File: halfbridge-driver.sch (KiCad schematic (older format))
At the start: 33 parts, among them U12 MGJ1, U13 MGJ1, U14 2ED020I12-F2

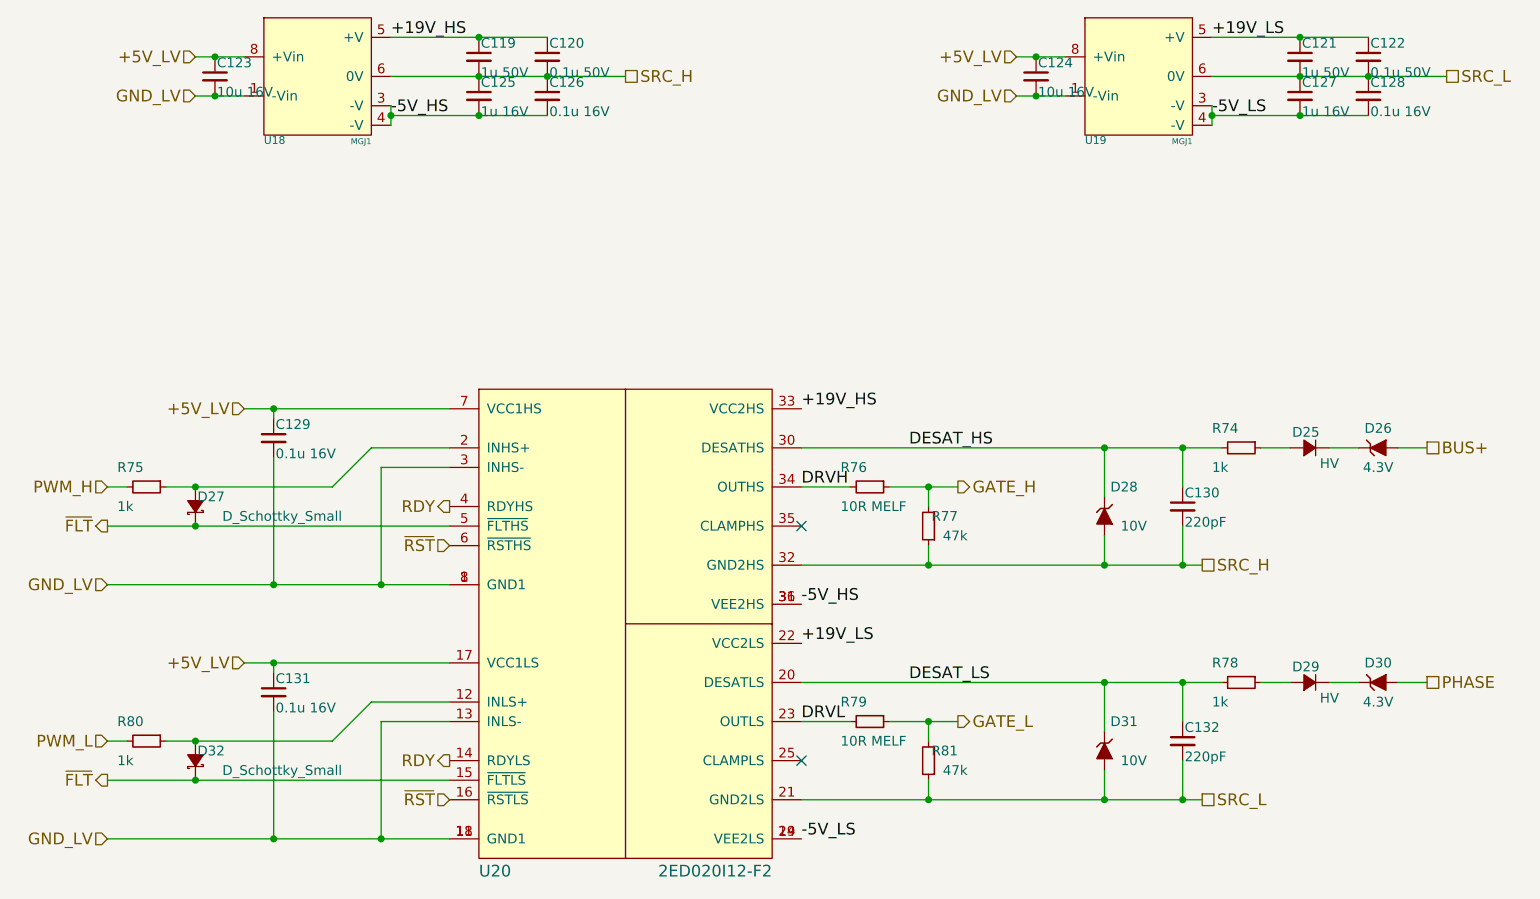
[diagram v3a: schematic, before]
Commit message: Add 1568 vias in DC link cap pads
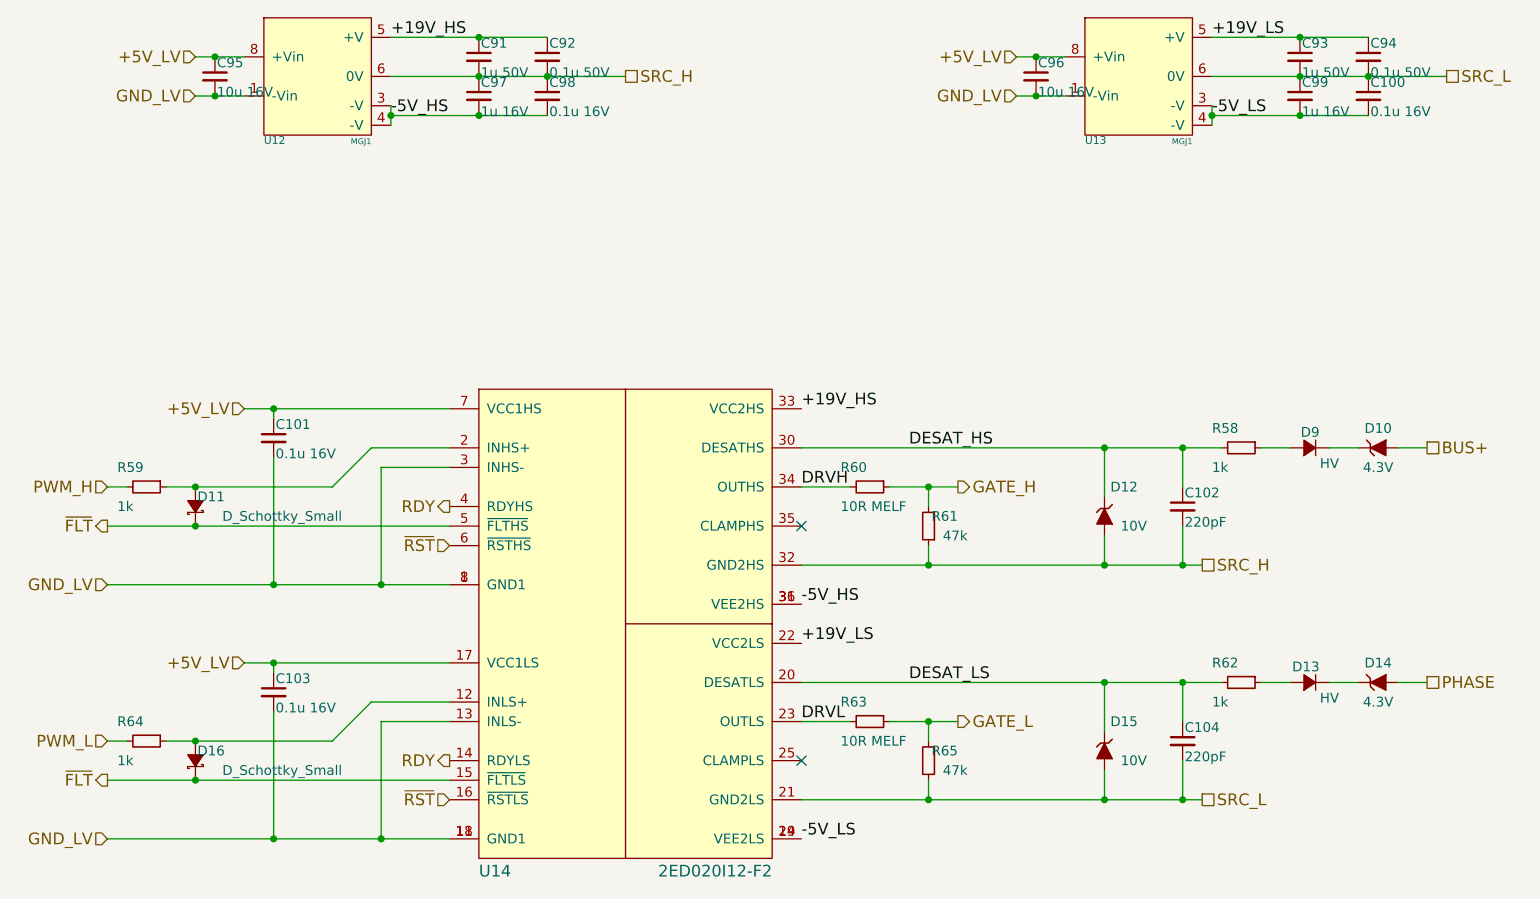
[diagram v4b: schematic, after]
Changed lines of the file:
@@
 AR Path="/57A1662D/57F260F4/57F02200" Ref="U17"  Part="1"
 AR Path="/57A1662D/57F2705F/57F02200" Ref="U20"  Part="1"
-F 0 "U20" H 4450 2750 60  0000 L BNN
+F 0 "U14" H 4450 2750 60  0000 L BNN
 F 1 "2ED020I12-F2" H 5950 2750 60  0000 R BNN
 F 2 "sictroller:PG-DSO-36-58" H 5200 4050 60  0001 C CNN
@@
 AR Path="/57A1662D/57F260F4/57F05C45" Ref="U15"  Part="1"
 AR Path="/57A1662D/57F2705F/57F05C45" Ref="U18"  Part="1"
-F 0 "U18" H 3350 900 40  0000 L BNN
+F 0 "U12" H 3350 900 40  0000 L BNN
 F 1 "MGJ1" H 3900 900 30  0000 R BNN
 F 2 "sictroller:MGJ1" H 3550 1250 60  0001 C CNN
@@
 AR Path="/57A1662D/57F260F4/57F05D03" Ref="C109"  Part="1"
 AR Path="/57A1662D/57F2705F/57F05D03" Ref="C123"  Part="1"
-F 0 "C123" H 3110 1320 50  0000 L CNN
+F 0 "C95" H 3110 1320 50  0000 L CNN
 F 1 "10u 16V" H 3110 1170 50  0000 L CNN
 F 2 "Capacitors_SMD:C_0805" H 3100 1250 50  0001 C CNN
@@
 AR Path="/57A1662D/57F260F4/57F05DBD" Ref="C105"  Part="1"
 AR Path="/57A1662D/57F2705F/57F05DBD" Ref="C119"  Part="1"
-F 0 "C119" H 4460 1220 50  0000 L CNN
+F 0 "C91" H 4460 1220 50  0000 L CNN
 F 1 "1u 50V" H 4460 1070 50  0000 L CNN
 F 2 "Capacitors_SMD:C_0805" H 4450 1150 50  0001 C CNN
@@
 AR Path="/57A1662D/57F260F4/57F05E19" Ref="C111"  Part="1"
 AR Path="/57A1662D/57F2705F/57F05E19" Ref="C125"  Part="1"
-F 0 "C125" H 4460 1420 50  0000 L CNN
+F 0 "C97" H 4460 1420 50  0000 L CNN
 F 1 "1u 16V" H 4460 1270 50  0000 L CNN
 F 2 "Capacitors_SMD:C_0603" H 4450 1350 50  0001 C CNN
@@
 AR Path="/57A1662D/57F260F4/57F0708D" Ref="U16"  Part="1"
 AR Path="/57A1662D/57F2705F/57F0708D" Ref="U19"  Part="1"
-F 0 "U19" H 7550 900 40  0000 L BNN
+F 0 "U13" H 7550 900 40  0000 L BNN
 F 1 "MGJ1" H 8100 900 30  0000 R BNN
 F 2 "sictroller:MGJ1" H 7750 1250 60  0001 C CNN
@@
 AR Path="/57A1662D/57F260F4/57F07093" Ref="C110"  Part="1"
 AR Path="/57A1662D/57F2705F/57F07093" Ref="C124"  Part="1"
-F 0 "C124" H 7310 1320 50  0000 L CNN
+F 0 "C96" H 7310 1320 50  0000 L CNN
 F 1 "10u 16V" H 7310 1170 50  0000 L CNN
 F 2 "Capacitors_SMD:C_0805" H 7300 1250 50  0001 C CNN
@@
 AR Path="/57A1662D/57F260F4/57F07099" Ref="C107"  Part="1"
 AR Path="/57A1662D/57F2705F/57F07099" Ref="C121"  Part="1"
-F 0 "C121" H 8660 1220 50  0000 L CNN
+F 0 "C93" H 8660 1220 50  0000 L CNN
 F 1 "1u 50V" H 8660 1070 50  0000 L CNN
 F 2 "Capacitors_SMD:C_0805" H 8650 1150 50  0001 C CNN
@@
 AR Path="/57A1662D/57F260F4/57F0709F" Ref="C113"  Part="1"
 AR Path="/57A1662D/57F2705F/57F0709F" Ref="C127"  Part="1"
-F 0 "C127" H 8660 1420 50  0000 L CNN
+F 0 "C99" H 8660 1420 50  0000 L CNN
 F 1 "1u 16V" H 8660 1270 50  0000 L CNN
 F 2 "Capacitors_SMD:C_0603" H 8650 1350 50  0001 C CNN
@@
 AR Path="/57A1662D/57F260F4/57F1574E" Ref="R68"  Part="1"
 AR Path="/57A1662D/57F2705F/57F1574E" Ref="R76"  Part="1"
-F 0 "R76" V 6350 3200 50  0000 L CNN
+F 0 "R60" V 6350 3200 50  0000 L CNN
 F 1 "10R MELF" V 6550 3200 50  0000 L CNN
 F 2 "sictroller:MELF-0204" H 6450 3350 50  0001 C CNN
@@
 AR Path="/57A1662D/57F260F4/57F16BC4" Ref="D17"  Part="1"
 AR Path="/57A1662D/57F2705F/57F16BC4" Ref="D25"  Part="1"
-F 0 "D25" H 8650 3230 50  0000 L CNN
+F 0 "D9" H 8650 3230 50  0000 L CNN
 F 1 "HV" H 8550 3070 50  0000 L CNN
 F 2 "Diodes_SMD:SMA_Standard" V 8700 3150 50  0001 C CNN
@@
 AR Path="/57A1662D/57F260F4/57F16C61" Ref="D18"  Part="1"
 AR Path="/57A1662D/57F2705F/57F16C61" Ref="D26"  Part="1"
-F 0 "D26" H 9050 3250 50  0000 C CNN
+F 0 "D10" H 9050 3250 50  0000 C CNN
 F 1 "4.3V" H 9050 3050 50  0000 C CNN
 F 2 "Diodes_SMD:SOD-523" H 9050 3150 50  0001 C CNN
@@
 AR Path="/57A1662D/57F260F4/57F16FB9" Ref="R66"  Part="1"
 AR Path="/57A1662D/57F2705F/57F16FB9" Ref="R74"  Part="1"
-F 0 "R74" V 8250 3000 50  0000 L CNN
+F 0 "R58" V 8250 3000 50  0000 L CNN
 F 1 "1k" V 8450 3000 50  0000 L CNN
 F 2 "Resistors_SMD:R_0402" H 8350 3150 50  0001 C CNN
@@
 AR Path="/57A1662D/57F260F4/57F17070" Ref="C116"  Part="1"
 AR Path="/57A1662D/57F2705F/57F17070" Ref="C130"  Part="1"
-F 0 "C130" H 8060 3520 50  0000 L CNN
+F 0 "C102" H 8060 3520 50  0000 L CNN
 F 1 "220pF" H 8060 3370 50  0000 L CNN
 F 2 "Capacitors_SMD:C_0402" H 8050 3450 50  0001 C CNN
@@
 AR Path="/57A1662D/57F260F4/57F185FE" Ref="R69"  Part="1"
 AR Path="/57A1662D/57F2705F/57F185FE" Ref="R77"  Part="1"
-F 0 "R77" H 6600 3500 50  0000 L CNN
+F 0 "R61" H 6600 3500 50  0000 L CNN
 F 1 "47k" H 6550 3600 50  0000 L CNN
 F 2 "Resistors_SMD:R_0805" H 6750 3550 50  0001 C CNN
@@
 AR Path="/57A1662D/57F260F4/57F1899B" Ref="D20"  Part="1"
 AR Path="/57A1662D/57F2705F/57F1899B" Ref="D28"  Part="1"
-F 0 "D28" V 7500 3600 50  0000 C CNN
+F 0 "D12" V 7500 3600 50  0000 C CNN
 F 1 "10V" V 7700 3650 50  0000 C CNN
 F 2 "Diodes_SMD:SOD-523" H 7650 3500 50  0001 C CNN
@@
 AR Path="/57A1662D/57F260F4/57F19BF8" Ref="R71"  Part="1"
 AR Path="/57A1662D/57F2705F/57F19BF8" Ref="R79"  Part="1"
-F 0 "R79" V 6350 4400 50  0000 L CNN
+F 0 "R63" V 6350 4400 50  0000 L CNN
 F 1 "10R MELF" V 6550 4400 50  0000 L CNN
 F 2 "sictroller:MELF-0204" H 6450 4550 50  0001 C CNN
@@
 AR Path="/57A1662D/57F260F4/57F19C08" Ref="D21"  Part="1"
 AR Path="/57A1662D/57F2705F/57F19C08" Ref="D29"  Part="1"
-F 0 "D29" H 8650 4430 50  0000 L CNN
+F 0 "D13" H 8650 4430 50  0000 L CNN
 F 1 "HV" H 8550 4270 50  0000 L CNN
 F 2 "Diodes_SMD:SMA_Standard" V 8700 4350 50  0001 C CNN
@@
 AR Path="/57A1662D/57F260F4/57F19C0E" Ref="D22"  Part="1"
 AR Path="/57A1662D/57F2705F/57F19C0E" Ref="D30"  Part="1"
-F 0 "D30" H 9050 4450 50  0000 C CNN
+F 0 "D14" H 9050 4450 50  0000 C CNN
 F 1 "4.3V" H 9050 4250 50  0000 C CNN
 F 2 "Diodes_SMD:SOD-523" H 9050 4350 50  0001 C CNN
@@
 AR Path="/57A1662D/57F260F4/57F19C16" Ref="R70"  Part="1"
 AR Path="/57A1662D/57F2705F/57F19C16" Ref="R78"  Part="1"
-F 0 "R78" V 8250 4200 50  0000 L CNN
+F 0 "R62" V 8250 4200 50  0000 L CNN
 F 1 "1k" V 8450 4200 50  0000 L CNN
 F 2 "Resistors_SMD:R_0402" H 8350 4350 50  0001 C CNN
@@
 AR Path="/57A1662D/57F260F4/57F19C1F" Ref="C118"  Part="1"
 AR Path="/57A1662D/57F2705F/57F19C1F" Ref="C132"  Part="1"
-F 0 "C132" H 8060 4720 50  0000 L CNN
+F 0 "C104" H 8060 4720 50  0000 L CNN
 F 1 "220pF" H 8060 4570 50  0000 L CNN
 F 2 "Capacitors_SMD:C_0402" H 8050 4650 50  0001 C CNN
@@
 AR Path="/57A1662D/57F260F4/57F19C2A" Ref="R73"  Part="1"
 AR Path="/57A1662D/57F2705F/57F19C2A" Ref="R81"  Part="1"
-F 0 "R81" H 6600 4700 50  0000 L CNN
+F 0 "R65" H 6600 4700 50  0000 L CNN
 F 1 "47k" H 6550 4800 50  0000 L CNN
 F 2 "Resistors_SMD:R_0805" H 6750 4750 50  0001 C CNN
@@
 AR Path="/57A1662D/57F260F4/57F19C34" Ref="D23"  Part="1"
 AR Path="/57A1662D/57F2705F/57F19C34" Ref="D31"  Part="1"
-F 0 "D31" V 7500 4800 50  0000 C CNN
+F 0 "D15" V 7500 4800 50  0000 C CNN
 F 1 "10V" V 7700 4850 50  0000 C CNN
 F 2 "Diodes_SMD:SOD-523" H 7650 4700 50  0001 C CNN
@@
 AR Path="/57A1662D/57F260F4/57F1A51C" Ref="C115"  Part="1"
 AR Path="/57A1662D/57F2705F/57F1A51C" Ref="C129"  Part="1"
-F 0 "C129" H 3410 3170 50  0000 L CNN
+F 0 "C101" H 3410 3170 50  0000 L CNN
 F 1 "0.1u 16V" H 3410 3020 50  0000 L CNN
 F 2 "Capacitors_SMD:C_0402" H 3400 3100 50  0001 C CNN
@@
 AR Path="/57A1662D/57F260F4/57F1C1CA" Ref="R67"  Part="1"
 AR Path="/57A1662D/57F2705F/57F1C1CA" Ref="R75"  Part="1"
-F 0 "R75" V 2650 3200 50  0000 L CNN
+F 0 "R59" V 2650 3200 50  0000 L CNN
 F 1 "1k" V 2850 3200 50  0000 L CNN
 F 2 "Resistors_SMD:R_0402" H 2750 3350 50  0001 C CNN
@@
 AR Path="/57A1662D/57F260F4/57F1C51E" Ref="D19"  Part="1"
 AR Path="/57A1662D/57F2705F/57F1C51E" Ref="D27"  Part="1"
-F 0 "D27" V 3050 3300 50  0000 L CNN
+F 0 "D11" V 3050 3300 50  0000 L CNN
 F 1 "D_Schottky_Small" V 2950 2700 50  0000 L CNN
 F 2 "Diodes_SMD:SOD-523" V 3000 3450 50  0001 C CNN
@@
 AR Path="/57A1662D/57F260F4/57F1DED1" Ref="C117"  Part="1"
 AR Path="/57A1662D/57F2705F/57F1DED1" Ref="C131"  Part="1"
-F 0 "C131" H 3410 4470 50  0000 L CNN
+F 0 "C103" H 3410 4470 50  0000 L CNN
 F 1 "0.1u 16V" H 3410 4320 50  0000 L CNN
 F 2 "Capacitors_SMD:C_0402" H 3400 4400 50  0001 C CNN
@@
 AR Path="/57A1662D/57F260F4/57F1DEE0" Ref="R72"  Part="1"
 AR Path="/57A1662D/57F2705F/57F1DEE0" Ref="R80"  Part="1"
-F 0 "R80" V 2650 4500 50  0000 L CNN
+F 0 "R64" V 2650 4500 50  0000 L CNN
 F 1 "1k" V 2850 4500 50  0000 L CNN
 F 2 "Resistors_SMD:R_0402" H 2750 4650 50  0001 C CNN
@@
 AR Path="/57A1662D/57F260F4/57F1DEE7" Ref="D24"  Part="1"
 AR Path="/57A1662D/57F2705F/57F1DEE7" Ref="D32"  Part="1"
-F 0 "D32" V 3050 4600 50  0000 L CNN
+F 0 "D16" V 3050 4600 50  0000 L CNN
 F 1 "D_Schottky_Small" V 2950 4000 50  0000 L CNN
 F 2 "Diodes_SMD:SOD-523" V 3000 4750 50  0001 C CNN
@@
 AR Path="/57A1662D/57F260F4/57FC6B04" Ref="C108"  Part="1"
 AR Path="/57A1662D/57F2705F/57FC6B04" Ref="C122"  Part="1"
-F 0 "C122" H 9010 1220 50  0000 L CNN
+F 0 "C94" H 9010 1220 50  0000 L CNN
 F 1 "0.1u 50V" H 9010 1070 50  0000 L CNN
 F 2 "Capacitors_SMD:C_0603" H 9000 1150 50  0001 C CNN
@@
 AR Path="/57A1662D/57F260F4/57FC6BF3" Ref="C114"  Part="1"
 AR Path="/57A1662D/57F2705F/57FC6BF3" Ref="C128"  Part="1"
-F 0 "C128" H 9010 1420 50  0000 L CNN
+F 0 "C100" H 9010 1420 50  0000 L CNN
 F 1 "0.1u 16V" H 9010 1270 50  0000 L CNN
 F 2 "Capacitors_SMD:C_0402" H 9000 1350 50  0001 C CNN
@@
 AR Path="/57A1662D/57F260F4/57FC72B1" Ref="C106"  Part="1"
 AR Path="/57A1662D/57F2705F/57FC72B1" Ref="C120"  Part="1"
-F 0 "C120" H 4810 1220 50  0000 L CNN
+F 0 "C92" H 4810 1220 50  0000 L CNN
 F 1 "0.1u 50V" H 4810 1070 50  0000 L CNN
 F 2 "Capacitors_SMD:C_0603" H 4800 1150 50  0001 C CNN
@@
 AR Path="/57A1662D/57F260F4/57FC72B7" Ref="C112"  Part="1"
 AR Path="/57A1662D/57F2705F/57FC72B7" Ref="C126"  Part="1"
-F 0 "C126" H 4810 1420 50  0000 L CNN
+F 0 "C98" H 4810 1420 50  0000 L CNN
 F 1 "0.1u 16V" H 4810 1270 50  0000 L CNN
 F 2 "Capacitors_SMD:C_0402" H 4800 1350 50  0001 C CNN
